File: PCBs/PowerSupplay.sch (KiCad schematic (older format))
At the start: 9 parts, among them J8 Jack-DC, U3 L7805, U5 LM1117-3.3

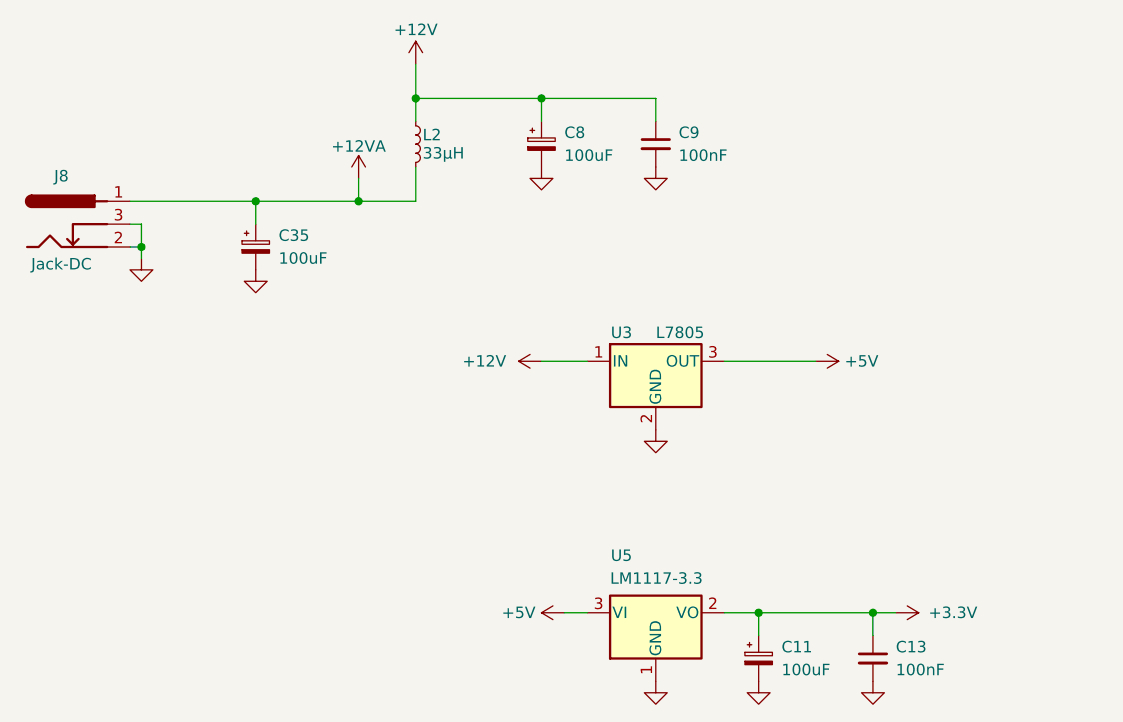
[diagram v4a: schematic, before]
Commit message: migrate to attiny1614
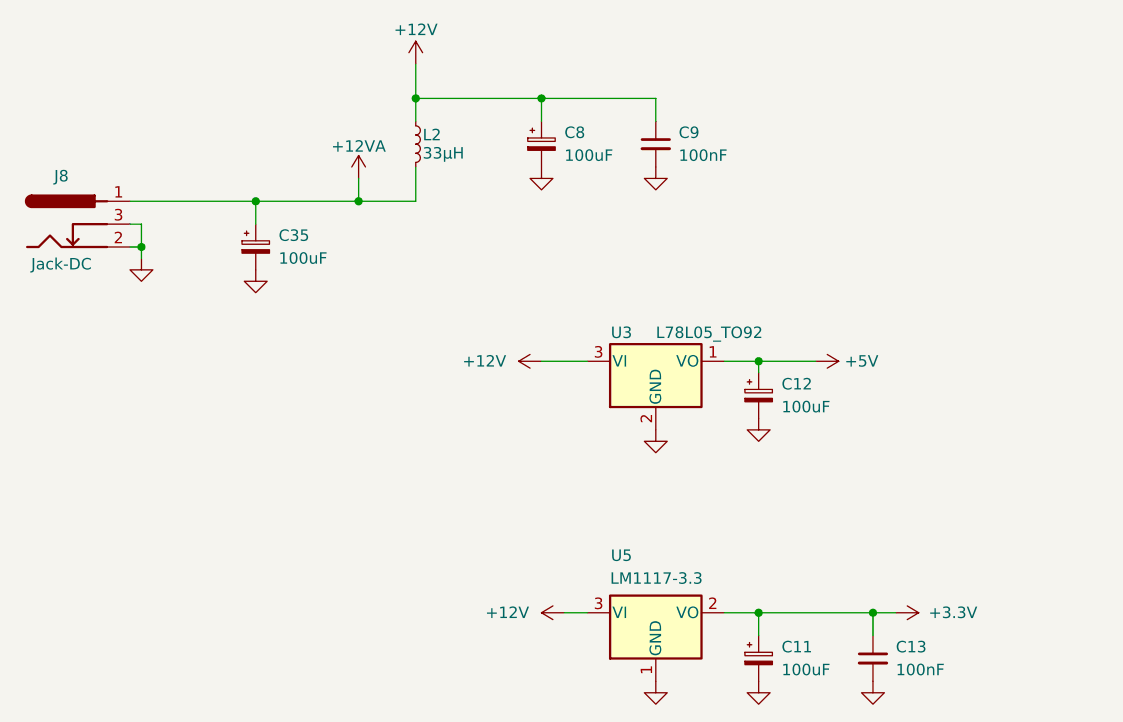
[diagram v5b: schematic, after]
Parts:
- removed U3: L7805, TO_SOT_Packages_THT:TO-220-3_Vertical, symbol L7805
- added C12: 100uF, Capacitors_THT:CP_Radial_D6.3mm_P2.50mm, symbol CP_Small
- added U3: L78L05_TO92, TO_SOT_Packages_THT:TO-92_Inline_Wide, symbol L78L05_TO92
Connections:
- net +12V: now also U5.3 (VI), U3.3 (VI)
- net +5V: now also C12.1, U3.1 (VO); no longer U5.3 (VI)
- net GND: now also C12.2, U3.2 (GND)
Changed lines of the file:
@@
 LIBS:Interface_USB
 LIBS:Arduino
+LIBS:MCU_Microchip_ATtiny
 LIBS:LCSDR-cache
 EELAYER 25 0
@@
 $EndComp
 $Comp
-L GND #PWR18
+L GND #PWR010
 U 1 1 6253C230
 P 3450 1550
-F 0 "#PWR18" H 3450 1300 50  0001 C CNN
+F 0 "#PWR010" H 3450 1300 50  0001 C CNN
 F 1 "GND" H 3450 1400 50  0001 C CNN
 F 2 "" H 3450 1550 50  0001 C CNN
@@
 $EndComp
 $Comp
-L GND #PWR21
+L GND #PWR011
 U 1 1 6253C236
 P 3950 1550
-F 0 "#PWR21" H 3950 1300 50  0001 C CNN
+F 0 "#PWR011" H 3950 1300 50  0001 C CNN
 F 1 "GND" H 3950 1400 50  0001 C CNN
 F 2 "" H 3950 1550 50  0001 C CNN
@@
 $EndComp
 $Comp
-L GND #PWR23
+L GND #PWR012
 U 1 1 6253C24A
 P 3950 3800
-F 0 "#PWR23" H 3950 3550 50  0001 C CNN
+F 0 "#PWR012" H 3950 3550 50  0001 C CNN
 F 1 "GND" H 3950 3650 50  0001 C CNN
 F 2 "" H 3950 3800 50  0001 C CNN
@@
 $EndComp
 $Comp
-L GND #PWR24
+L GND #PWR013
 U 1 1 6253C257
 P 4400 3800
-F 0 "#PWR24" H 4400 3550 50  0001 C CNN
+F 0 "#PWR013" H 4400 3550 50  0001 C CNN
 F 1 "GND" H 4400 3650 50  0001 C CNN
 F 2 "" H 4400 3800 50  0001 C CNN
@@
 $EndComp
 $Comp
-L GND #PWR26
+L GND #PWR014
 U 1 1 6253C25D
 P 4900 3800
-F 0 "#PWR26" H 4900 3550 50  0001 C CNN
+F 0 "#PWR014" H 4900 3550 50  0001 C CNN
 F 1 "GND" H 4900 3650 50  0001 C CNN
 F 2 "" H 4900 3800 50  0001 C CNN
@@
 $EndComp
 $Comp
-L +3.3V #PWR27
+L +3.3V #PWR015
 U 1 1 6253C26A
 P 5000 3500
-F 0 "#PWR27" H 5000 3350 50  0001 C CNN
+F 0 "#PWR015" H 5000 3350 50  0001 C CNN
 F 1 "+3.3V" V 5000 3750 50  0000 C CNN
 F 2 "" H 5000 3500 50  0001 C CNN
@@
 $EndComp
 $Comp
-L GND #PWR14
+L GND #PWR016
 U 1 1 6253C290
 P 1700 1950
-F 0 "#PWR14" H 1700 1700 50  0001 C CNN
+F 0 "#PWR016" H 1700 1700 50  0001 C CNN
 F 1 "GND" H 1700 1800 50  0001 C CNN
 F 2 "" H 1700 1950 50  0001 C CNN
@@
 	2900 1100 2900 1350
 $Comp
-L +12VA #PWR16
+L +12VA #PWR017
 U 1 1 630BADB5
 P 2650 1600
-F 0 "#PWR16" H 2650 1450 50  0001 C CNN
+F 0 "#PWR017" H 2650 1450 50  0001 C CNN
 F 1 "+12VA" H 2650 1740 50  0000 C CNN
 F 2 "" H 2650 1600 50  0001 C CNN
@@
 $EndComp
 $Comp
-L GND #PWR15
+L GND #PWR018
 U 1 1 630BB4AD
 P 2200 2000
-F 0 "#PWR15" H 2200 1750 50  0001 C CNN
+F 0 "#PWR018" H 2200 1750 50  0001 C CNN
 F 1 "GND" H 2200 1850 50  0001 C CNN
 F 2 "" H 2200 2000 50  0001 C CNN
@@
 	3550 3500 3650 3500
 $Comp
-L +12V #PWR17
+L +12V #PWR019
 U 1 1 638424E1
 P 2900 1100
-F 0 "#PWR17" H 2900 950 50  0001 C CNN
+F 0 "#PWR019" H 2900 950 50  0001 C CNN
 F 1 "+12V" H 2900 1250 50  0000 C CNN
 F 2 "" H 2900 1100 50  0001 C CNN
@@
 $EndComp
 $Comp
-L L7805 U3
-U 1 1 639E7452
-P 3950 2400
-F 0 "U3" H 3800 2525 50  0000 C CNN
-F 1 "L7805" H 3950 2525 50  0000 L CNN
-F 2 "TO_SOT_Packages_THT:TO-220-3_Vertical" H 3975 2250 50  0001 L CIN
-F 3 "" H 3950 2350 50  0001 C CNN
-	1    3950 2400
-	1    0    0    -1
-$EndComp
-$Comp
-L +12V #PWR19
+L +12V #PWR020
 U 1 1 639E751B
 P 3450 2400
-F 0 "#PWR19" H 3450 2250 50  0001 C CNN
+F 0 "#PWR020" H 3450 2250 50  0001 C CNN
 F 1 "+12V" V 3450 2650 50  0000 C CNN
 F 2 "" H 3450 2400 50  0001 C CNN
@@
 	3450 2400 3650 2400
 $Comp
-L GND #PWR22
+L GND #PWR021
 U 1 1 639E7562
 P 3950 2700
-F 0 "#PWR22" H 3950 2450 50  0001 C CNN
+F 0 "#PWR021" H 3950 2450 50  0001 C CNN
 F 1 "GND" H 3950 2550 50  0001 C CNN
 F 2 "" H 3950 2700 50  0001 C CNN
@@
 	4250 2400 4650 2400
 $Comp
-L +5V #PWR25
+L +5V #PWR022
 U 1 1 639E7652
 P 4650 2400
-F 0 "#PWR25" H 4650 2250 50  0001 C CNN
+F 0 "#PWR022" H 4650 2250 50  0001 C CNN
 F 1 "+5V" V 4650 2600 50  0000 C CNN
 F 2 "" H 4650 2400 50  0001 C CNN
@@
 $EndComp
 $Comp
-L +5V #PWR20
-U 1 1 639E76B5
+L L78L05_TO92 U3
+U 1 1 63B71A5A
+P 3950 2400
+F 0 "U3" H 3800 2525 50  0000 C CNN
+F 1 "L78L05_TO92" H 3950 2525 50  0000 L CNN
+F 2 "TO_SOT_Packages_THT:TO-92_Inline_Wide" H 3950 2625 50  0001 C CIN
+F 3 "" H 3950 2350 50  0001 C CNN
+	1    3950 2400
+	1    0    0    -1
+$EndComp
+$Comp
+L +12V #PWR023
+U 1 1 63B71AC9
 P 3550 3500
-F 0 "#PWR20" H 3550 3350 50  0001 C CNN
-F 1 "+5V" V 3550 3700 50  0000 C CNN
+F 0 "#PWR023" H 3550 3350 50  0001 C CNN
+F 1 "+12V" V 3550 3750 50  0000 C CNN
 F 2 "" H 3550 3500 50  0001 C CNN
 F 3 "" H 3550 3500 50  0001 C CNN
@@
 	0    -1   -1   0
 $EndComp
+$Comp
+L CP_Small C12
+U 1 1 63B71B25
+P 4400 2550
+F 0 "C12" H 4500 2600 50  0000 L CNN
+F 1 "100uF" H 4500 2500 50  0000 L CNN
+F 2 "Capacitors_THT:CP_Radial_D6.3mm_P2.50mm" H 4400 2550 50  0001 C CNN
+F 3 "" H 4400 2550 50  0001 C CNN
+	1    4400 2550
+	1    0    0    -1
+$EndComp
+Wire Wire Line
+	4400 2450 4400 2400
+Connection ~ 4400 2400
+$Comp
+L GND #PWR024
+U 1 1 63B71BE6
+P 4400 2650
+F 0 "#PWR024" H 4400 2400 50  0001 C CNN
+F 1 "GND" H 4400 2500 50  0001 C CNN
+F 2 "" H 4400 2650 50  0001 C CNN
+F 3 "" H 4400 2650 50  0001 C CNN
+	1    4400 2650
+	1    0    0    -1
+$EndComp
 $EndSCHEMATC
